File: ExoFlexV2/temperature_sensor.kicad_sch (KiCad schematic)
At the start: 26 parts, among them U66 ADCMP602BRMZ, U67 ADCMP602BRMZ, U68 SN74LVC1G32DBVR

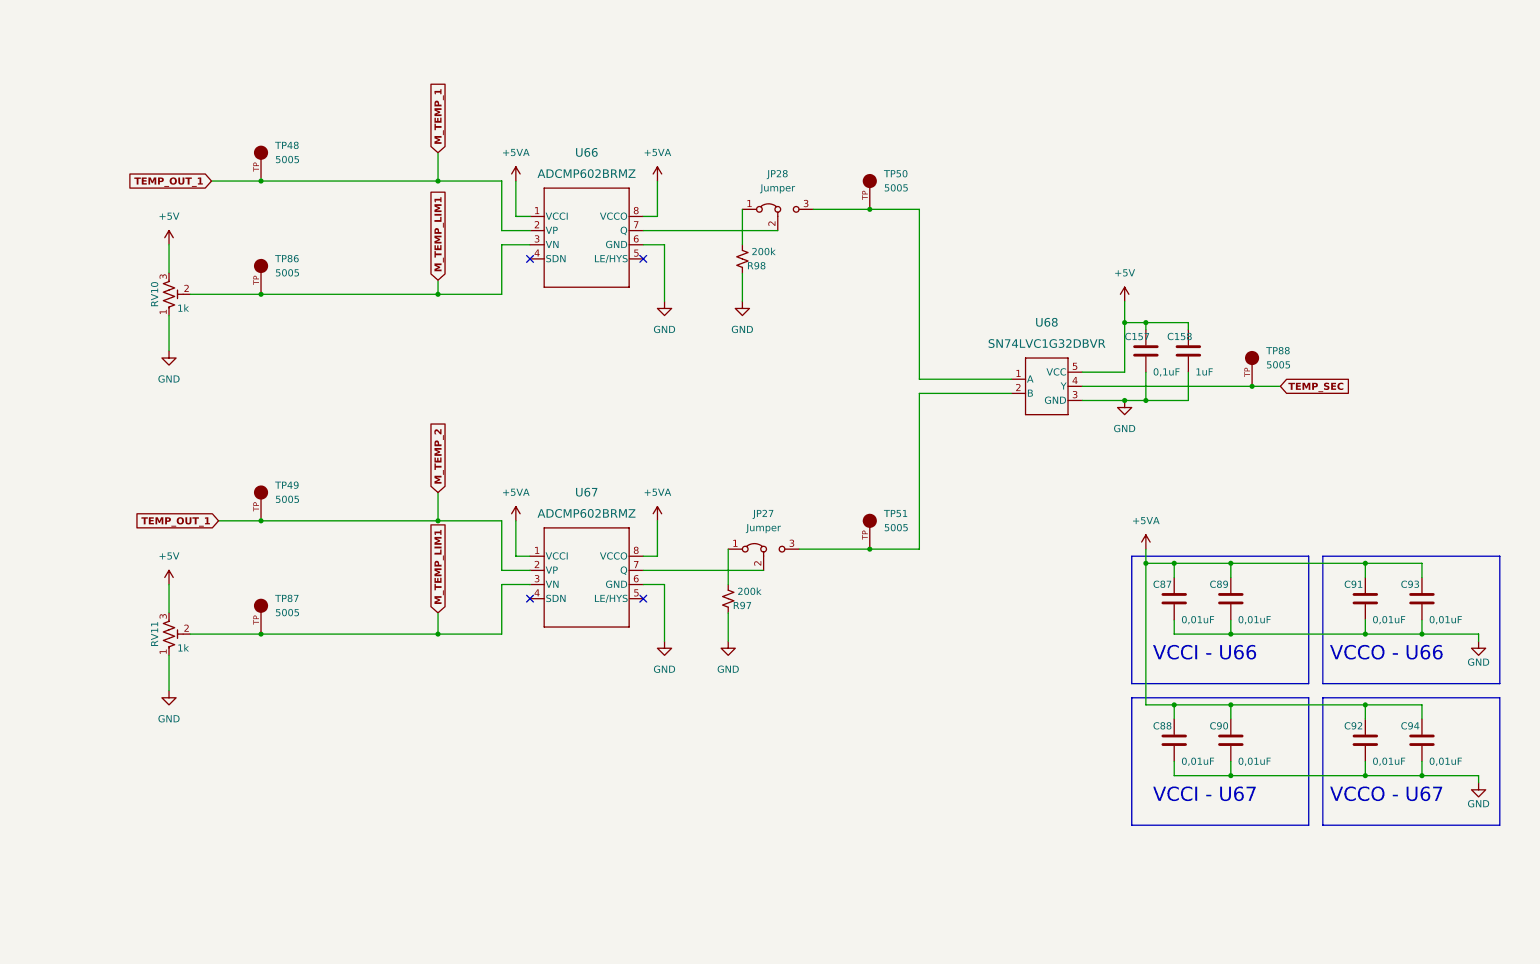
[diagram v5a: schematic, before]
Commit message: Finalisation 1
- Ajout de pages pour la gestion des signaux négatif
- Modification des pages de torque et amplitude
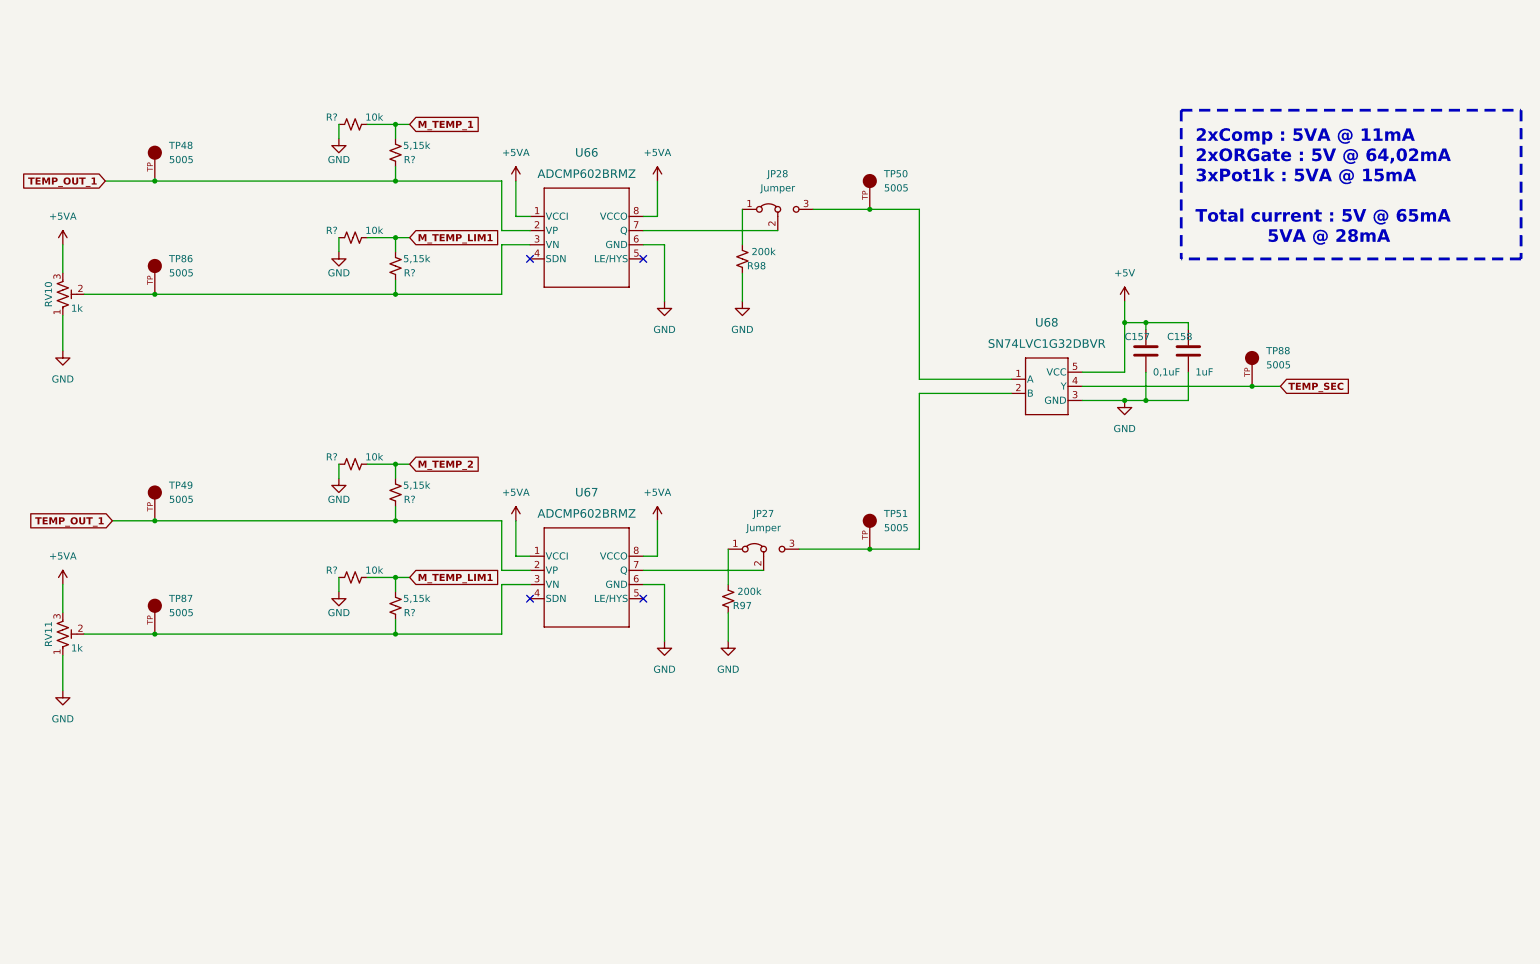
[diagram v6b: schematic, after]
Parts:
- removed C87, C88, C89, C90, C91, C92, C93, C94: 0,01uF, Capacitor_SMD:C_0603_1608Metric, symbol Device:C
- added R? (x4): 5,15k, Resistor_SMD:R_0805_2012Metric, symbol Device:R_Small_US
- added R? (x4): 10k, Resistor_SMD:R_0805_2012Metric, symbol Device:R_Small_US
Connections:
- net +5V: no longer RV10.3, RV11.3
- net +5VA: now also RV10.3, RV11.3
- net GND: now also R?.1, R?.1, R?.1, R?.1
- net M_TEMP_1: now also R?.1, R?.2; no longer TP48.TP, TP49.TP, U66.2 (VP), U67.2 (VP)
- net M_TEMP_LIM1: now also R?.1, R?.1, R?.2, R?.2; no longer RV10.2, RV11.2, TP86.TP, TP87.TP, U66.3 (VN), U67.3 (VN)
- new net: R?.2, RV10.2, TP86.TP, U66.3 (VN)
- new net: R?.2, RV11.2, TP87.TP, U67.3 (VN)
- new net M_TEMP_2: R?.1, R?.2
- new net TEMP_OUT_1: R?.2, R?.2, TP48.TP, TP49.TP, U66.2 (VP), U67.2 (VP)
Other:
- note added: "2xComp : 5VA @ 11mA 2xORGate : 5V @ 64,02mA 3xPot1k : 5VA @ 15mA Total current : 5V @ 65mA 5VA @ 28mA"
- note removed: "VCCI - U66"
- note removed: "VCCI - U67"
- note removed: "VCCO - U66"
- note removed: "VCCO - U67"
- moved on the sheet: RV10, RV11, TP48, TP49, TP86, TP87
